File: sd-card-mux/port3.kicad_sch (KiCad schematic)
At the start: 10 parts, among them J201 47309-2285, U201 74LVC1G3157, U202 74LVC1G3157, U203 74LVC1G3157, U204 74LVC1G3157, U205 74LVC1G3157, U206 74LVC1G3157

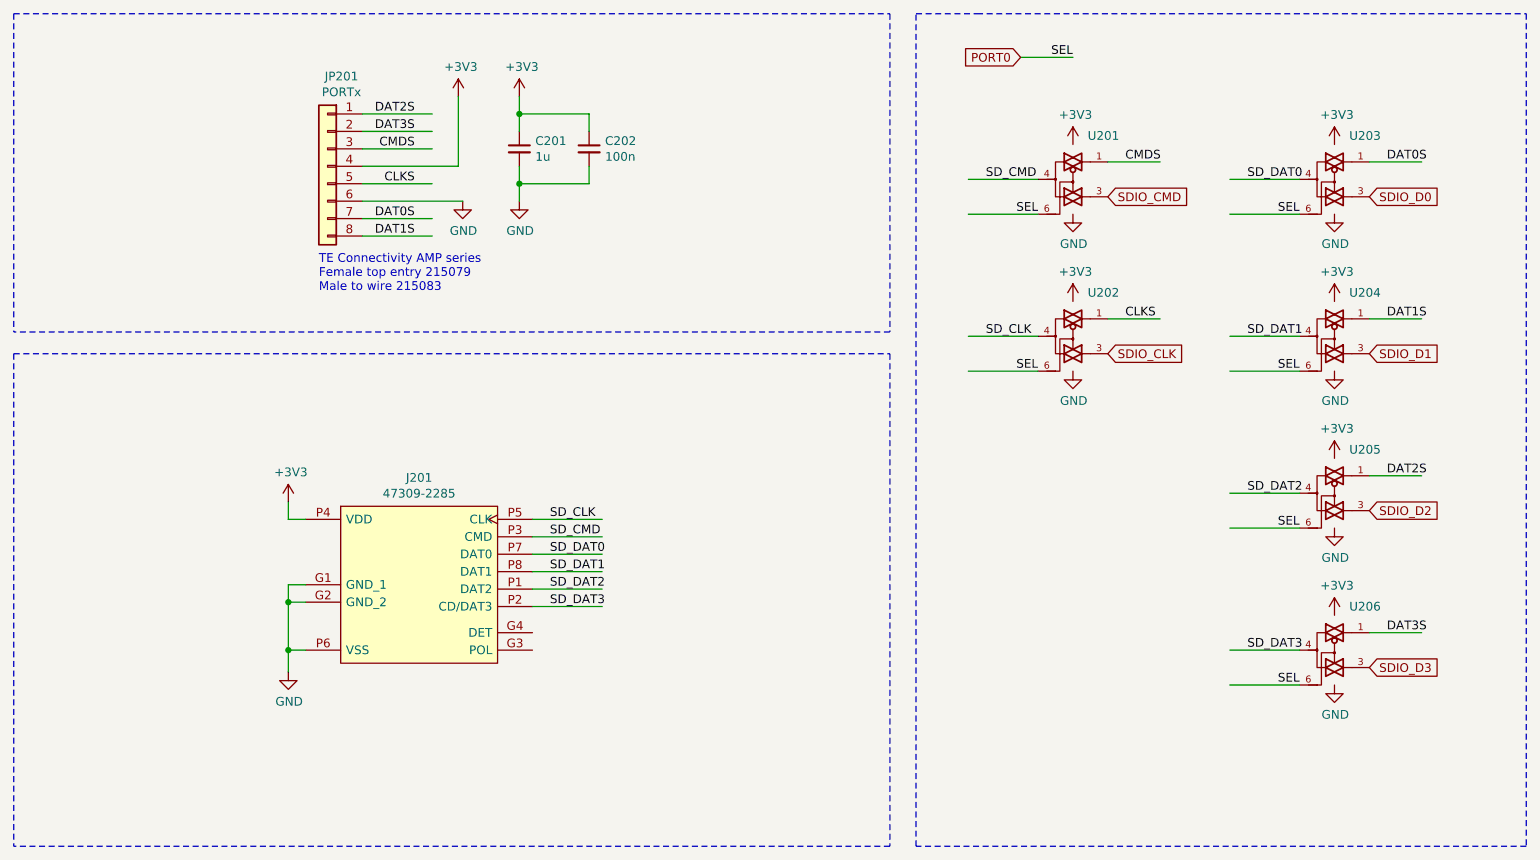
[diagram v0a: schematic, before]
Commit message: Added MCP23008 alternative
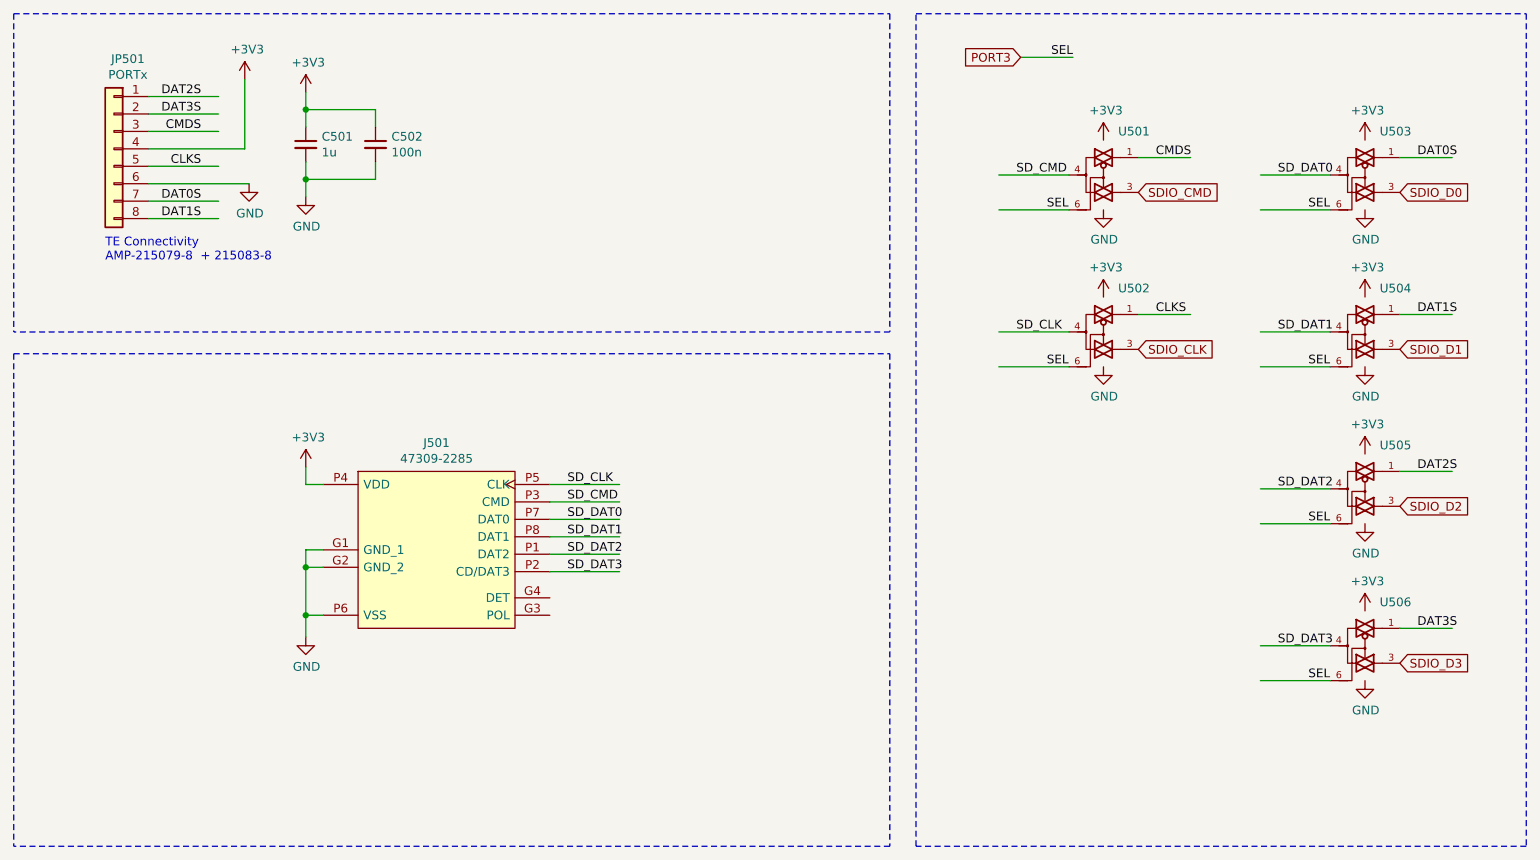
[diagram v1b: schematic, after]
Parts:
- removed C201: 1u, Capacitor_SMD:C_0402_1005Metric, symbol Device:C_Small
- removed C202: 100n, Capacitor_SMD:C_0402_1005Metric, symbol Device:C_Small
- removed J201: 47309-2285, footprints:47309-2285, symbol 47309-2285:47309-2285
- removed JP201: PORTx, Connector_JST:JST_PH_S8B-PH-K_1x08_P2.00mm_Horizontal, symbol Connector_Generic:Conn_01x08
- removed U201, U202, U203, U204, U205, U206: 74LVC1G3157, Package_TO_SOT_SMD:SOT-363_SC-70-6, symbol 74LVC1G3157:74LVC1G3157
- added C501: 1u, Capacitor_SMD:C_0402_1005Metric, symbol Device:C_Small
- added C502: 100n, Capacitor_SMD:C_0402_1005Metric, symbol Device:C_Small
- added J501: 47309-2285, footprints:47309-2285, symbol 47309-2285:47309-2285
- added JP501: PORTx, Connector_JST:JST_PH_S8B-PH-K_1x08_P2.00mm_Horizontal, symbol Connector_Generic:Conn_01x08
- added U501, U502, U503, U504, U505, U506: 74LVC1G3157, Package_TO_SOT_SMD:SOT-363_SC-70-6, symbol 74LVC1G3157:74LVC1G3157
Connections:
- net +3V3: now also C501.1, C502.1, J501.P4 (VDD), JP501.4 (Pin_4), U501.5 (VCC), U502.5 (VCC), U503.5 (VCC), U504.5 (VCC), U505.5 (VCC), U506.5 (VCC)
- net CLKS: now also JP501.5 (Pin_5), U502.1
- net CMDS: now also JP501.3 (Pin_3), U501.1
- net DAT0S: now also JP501.7 (Pin_7), U503.1
- net DAT1S: now also JP501.8 (Pin_8), U504.1
- net DAT2S: now also JP501.1 (Pin_1), U505.1
- net DAT3S: now also JP501.2 (Pin_2), U506.1
- net GND: now also C501.2, C502.2, J501.G1 (GND_1), J501.G2 (GND_2), J501.P6 (VSS), JP501.6 (Pin_6), U501.2 (GND), U502.2 (GND), U503.2 (GND), U504.2 (GND), U505.2 (GND), U506.2 (GND)
- net SDIO_CLK: now also U502.3
- net SDIO_CMD: now also U501.3
- net SDIO_D0: now also U503.3
- net SDIO_D1: now also U504.3
- net SDIO_D2: now also U505.3
- net SDIO_D3: now also U506.3
- net SD_CLK: now also J501.P5 (CLK), U502.4
- net SD_CMD: now also J501.P3 (CMD), U501.4
- net SD_DAT0: now also J501.P7 (DAT0), U503.4
- net SD_DAT1: now also J501.P8 (DAT1), U504.4
- net SD_DAT2: now also J501.P1 (DAT2), U505.4
- net SD_DAT3: now also J501.P2 (CD/DAT3), U506.4
- new net PORT3: U501.6, U502.6, U503.6, U504.6, U505.6, U506.6
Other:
- note added: "TE Connectivity AMP-215079-8 + 215083-8"
- note removed: "TE Connectivity AMP series Female top entry 215079 Male to wire 215083"

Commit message: Addedd missing upload port
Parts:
- C501: LCSC Part# (none) -> C52923
- C502: LCSC Part# (none) -> C1525
- JP501: footprint Connector_JST:JST_PH_S8B-PH-K_1x08_P2.00mm_Horizontal -> footprints:ConnectorMicromatch-8
- U501, U502, U503, U504, U505, U506: LCSC Part# (none) -> C38663
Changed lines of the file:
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@@
+      (effects (font (size 1.27 1.27)) hide)
+    )
+    (property "LCSC Part#" "C52923" (id 4) (at 63.5 38.1 0)
       (effects (font (size 1.27 1.27)) hide)
     )
@@
       (effects (font (size 1.27 1.27)) hide)
     )
+    (property "LCSC Part#" "C1525" (id 4) (at 73.66 38.1 0)
+      (effects (font (size 1.27 1.27)) hide)
+    )
   )
   (symbol (lib_name "74LVC1G3157:74LVC1G3157_2") (lib_id "74LVC1G3157:74LVC1G3157") (at 179.705 42.545 0) (unit 1)
@@
     )
     (property "Datasheet" "https://www.ti.com/lit/ds/symlink/sn74lvc1g3157.pdf" (id 3) (at 179.705 42.545 0)
+      (effects (font (size 1.27 1.27)) hide)
+    )
+    (property "LCSC Part#" " C38663" (id 4) (at 179.705 42.545 0)
       (effects (font (size 1.27 1.27)) hide)
     )
@@
       (effects (font (size 1.27 1.27)) hide)
     )
+    (property "LCSC Part#" " C38663" (id 4) (at 179.705 65.405 0)
+      (effects (font (size 1.27 1.27)) hide)
+    )
   )
   (symbol (lib_id "74LVC1G3157:74LVC1G3157") (at 217.805 42.545 0) (unit 1)
@@
     )
     (property "Datasheet" "https://www.ti.com/lit/ds/symlink/sn74lvc1g3157.pdf" (id 3) (at 217.805 42.545 0)
+      (effects (font (size 1.27 1.27)) hide)
+    )
+    (property "LCSC Part#" " C38663" (id 4) (at 217.805 42.545 0)
       (effects (font (size 1.27 1.27)) hide)
     )
@@
       (effects (font (size 1.27 1.27)) hide)
     )
+    (property "LCSC Part#" " C38663" (id 4) (at 217.805 65.405 0)
+      (effects (font (size 1.27 1.27)) hide)
+    )
   )
   (symbol (lib_id "74LVC1G3157:74LVC1G3157") (at 217.805 88.265 0) (unit 1)
@@
     )
     (property "Datasheet" "https://www.ti.com/lit/ds/symlink/sn74lvc1g3157.pdf" (id 3) (at 217.805 88.265 0)
+      (effects (font (size 1.27 1.27)) hide)
+    )
+    (property "LCSC Part#" " C38663" (id 4) (at 217.805 88.265 0)
       (effects (font (size 1.27 1.27)) hide)
     )
@@
       (effects (font (size 1.27 1.27)) hide)
     )
+    (property "LCSC Part#" " C38663" (id 4) (at 217.805 111.125 0)
+      (effects (font (size 1.27 1.27)) hide)
+    )
   )
   (symbol (lib_id "Connector_Generic:Conn_01x08") (at 35.56 38.735 0) (mirror y) (unit 1)
@@
     (property "Reference" "JP501" (id 0) (at 37.592 25.635 0))
     (property "Value" "PORTx" (id 1) (at 37.592 27.9335 0))
-    (property "Footprint" "Connector_JST:JST_PH_S8B-PH-K_1x08_P2.00mm_Horizontal" (id 2) (at 35.56 38.735 0)
+    (property "Footprint" "footprints:ConnectorMicromatch-8" (id 2) (at 35.56 38.735 0)
       (effects (font (size 1.27 1.27)) hide)
     )

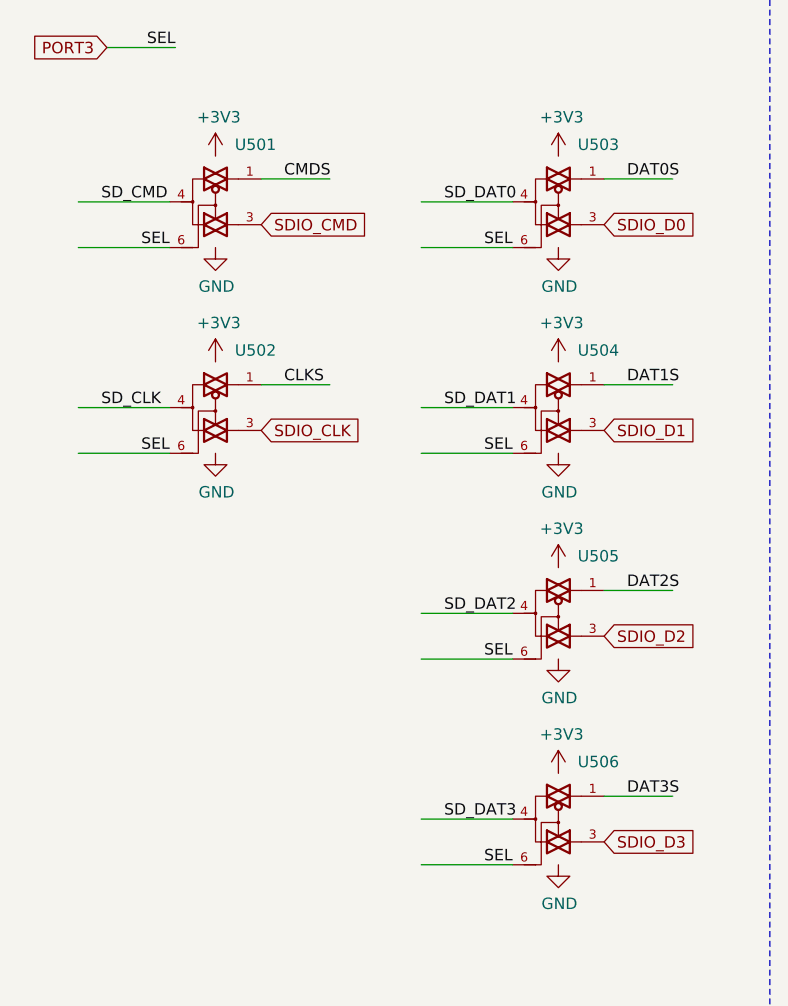
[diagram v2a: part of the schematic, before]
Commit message: Correction of inverted pins
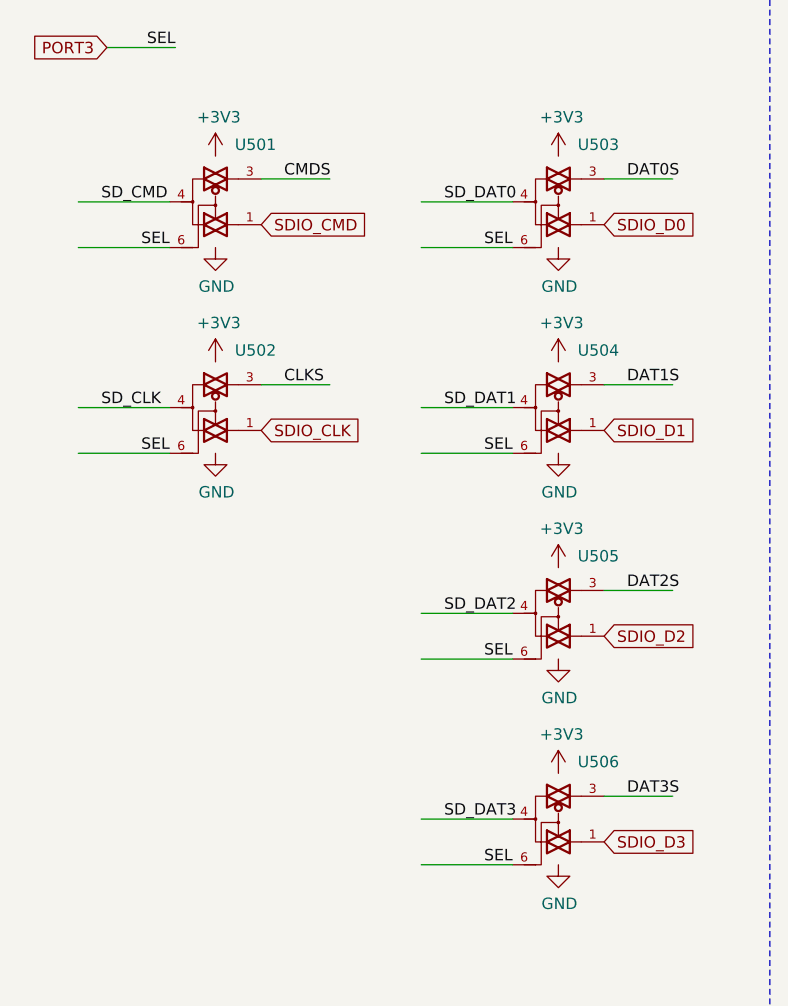
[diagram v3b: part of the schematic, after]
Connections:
- net CLKS: now also U502.3; no longer U502.1
- net CMDS: now also U501.3; no longer U501.1
- net DAT0S: now also U503.3; no longer U503.1
- net DAT1S: now also U504.3; no longer U504.1
- net DAT2S: now also U505.3; no longer U505.1
- net DAT3S: now also U506.3; no longer U506.1
- net SDIO_CLK: now also U502.1; no longer U502.3
- net SDIO_CMD: now also U501.1; no longer U501.3
- net SDIO_D0: now also U503.1; no longer U503.3
- net SDIO_D1: now also U504.1; no longer U504.3
- net SDIO_D2: now also U505.1; no longer U505.3
- net SDIO_D3: now also U506.1; no longer U506.3
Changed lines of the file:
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@@
 (kicad_sch (version 20200608) (host eeschema "(5.99.0-1973-g8c57821e9)")
-  (page 1 9)
+  (page 5 9)
   (paper "A4")
   (junction (at 63.5 33.02))
@@
     )
   )
-  (symbol (lib_id "74LVC1G3157:74LVC1G3157") (at 217.805 42.545 0) (unit 1)
+  (symbol (lib_name "74LVC1G3157:74LVC1G3157_3") (lib_id "74LVC1G3157:74LVC1G3157") (at 217.805 42.545 0) (unit 1)
     (in_bom yes) (on_board yes)
     (property "Reference" "U503" (id 0) (at 222.25 36.195 0))
@@
     )
   )
-  (symbol (lib_id "74LVC1G3157:74LVC1G3157") (at 217.805 65.405 0) (unit 1)
+  (symbol (lib_name "74LVC1G3157:74LVC1G3157_4") (lib_id "74LVC1G3157:74LVC1G3157") (at 217.805 65.405 0) (unit 1)
     (in_bom yes) (on_board yes)
     (property "Reference" "U504" (id 0) (at 222.25 59.055 0))
@@
     )
   )
-  (symbol (lib_id "74LVC1G3157:74LVC1G3157") (at 217.805 88.265 0) (unit 1)
+  (symbol (lib_name "74LVC1G3157:74LVC1G3157_5") (lib_id "74LVC1G3157:74LVC1G3157") (at 217.805 88.265 0) (unit 1)
     (in_bom yes) (on_board yes)
     (property "Reference" "U505" (id 0) (at 222.25 81.915 0))

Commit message: Removal of host port and preparation for manufacturing
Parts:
- J501: Mechanical (none) -> T
- JP501: Mechanical (none) -> T; TME Part# (none) -> MM2x5
- U501, U502, U503, U504, U505, U506: LCSC Part# C38663 -> C265126; Rotation (none) -> 0
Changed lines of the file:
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@@
       (effects (font (size 1.27 1.27)) hide)
     )
-    (property "LCSC Part#" " C38663" (id 4) (at 179.705 42.545 0)
+    (property "LCSC Part#" "C265126" (id 4) (at 179.705 42.545 0)
+      (effects (font (size 1.27 1.27)) hide)
+    )
+    (property "Rotation" "0" (id 4) (at 179.705 42.545 0)
       (effects (font (size 1.27 1.27)) hide)
     )
@@
       (effects (font (size 1.27 1.27)) hide)
     )
-    (property "LCSC Part#" " C38663" (id 4) (at 179.705 65.405 0)
+    (property "LCSC Part#" "C265126" (id 4) (at 179.705 65.405 0)
+      (effects (font (size 1.27 1.27)) hide)
+    )
+    (property "Rotation" "0" (id 4) (at 179.705 65.405 0)
       (effects (font (size 1.27 1.27)) hide)
     )
@@
       (effects (font (size 1.27 1.27)) hide)
     )
-    (property "LCSC Part#" " C38663" (id 4) (at 217.805 42.545 0)
+    (property "LCSC Part#" "C265126" (id 4) (at 217.805 42.545 0)
+      (effects (font (size 1.27 1.27)) hide)
+    )
+    (property "Rotation" "0" (id 4) (at 217.805 42.545 0)
       (effects (font (size 1.27 1.27)) hide)
     )
@@
       (effects (font (size 1.27 1.27)) hide)
     )
-    (property "LCSC Part#" " C38663" (id 4) (at 217.805 65.405 0)
+    (property "LCSC Part#" "C265126" (id 4) (at 217.805 65.405 0)
+      (effects (font (size 1.27 1.27)) hide)
+    )
+    (property "Rotation" "0" (id 4) (at 217.805 65.405 0)
       (effects (font (size 1.27 1.27)) hide)
     )
@@
       (effects (font (size 1.27 1.27)) hide)
     )
-    (property "LCSC Part#" " C38663" (id 4) (at 217.805 88.265 0)
+    (property "LCSC Part#" "C265126" (id 4) (at 217.805 88.265 0)
+      (effects (font (size 1.27 1.27)) hide)
+    )
+    (property "Rotation" "0" (id 4) (at 217.805 88.265 0)
       (effects (font (size 1.27 1.27)) hide)
     )
@@
       (effects (font (size 1.27 1.27)) hide)
     )
-    (property "LCSC Part#" " C38663" (id 4) (at 217.805 111.125 0)
+    (property "LCSC Part#" "C265126" (id 4) (at 217.805 111.125 0)
+      (effects (font (size 1.27 1.27)) hide)
+    )
+    (property "Rotation" "0" (id 4) (at 217.805 111.125 0)
       (effects (font (size 1.27 1.27)) hide)
     )
@@
     )
     (property "Datasheet" "~" (id 3) (at 35.56 38.735 0)
+      (effects (font (size 1.27 1.27)) hide)
+    )
+    (property "TME Part#" "MM2x5" (id 4) (at 35.56 38.735 0)
+      (effects (font (size 1.27 1.27)) hide)
+    )
+    (property "Mechanical" "T" (id 4) (at 35.56 38.735 0)
       (effects (font (size 1.27 1.27)) hide)
     )
@@
       (effects (font (size 1.27 1.27)) (justify left) hide)
     )
+    (property "Mechanical" "T" (id 4) (at 66.04 88.265 0)
+      (effects (font (size 1.27 1.27)) hide)
+    )
   )
